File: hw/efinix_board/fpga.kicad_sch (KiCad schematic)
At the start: 1 part, among them U1 T20F256

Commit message: Start working on sdram
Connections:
- net ~{CAS}: now reaches U1.H12 (GPIOR_139)
- net ~{WE}: now reaches U1.J12 (GPIOR_141)
- net A4: now reaches U1.J13 (GPIOR_133)
- net A5: now reaches U1.J14 (GPIOR_135)
- net A6: now reaches U1.J15 (GPIOR_131)
- net A7: now reaches U1.K12 (GPIOR_148)
- net A8: now reaches U1.K14 (GPIOR_138)
- net DQ8: now reaches U1.K15 (GPIOR_136)
- net UQDM: now reaches U1.K16 (GPIOR_132)
- net A9: now reaches U1.L15 (GPIOR_147)
- net A11: now reaches U1.L16 (GPIOR_143)
- net A12: now reaches U1.M15 (GPIOR_144)
- net ~{CKE}: now reaches U1.M16 (GPIOR_145)
- net CLK: now reaches U1.P16 (GPIOR_146)
- net DQ6: now reaches U1.A11 (GPIOR_84)
- net DQ3: now reaches U1.A13 (GPIOR_95)
- net DQ1: now reaches U1.A14 (GPIOR_90)
- net DQ15: now reaches U1.A15 (GPIOR_94)
- net DQ7: now reaches U1.B10 (GPIOR_82)
- net DQ5: now reaches U1.B11 (GPIOR_83)
- net DQ4: now reaches U1.B12 (GPIOR_93)
- net DQ2: now reaches U1.B13 (GPIOR_97)
- net DQ0: now reaches U1.B14 (GPIOR_92)
- net DQ14: now reaches U1.B15 (GPIOR_98)
- net DQ13: now reaches U1.B16 (GPIOR_106)
- net LQDM: now reaches U1.B9 (GPIOR_80)
- net A2: now reaches U1.C11 (GPIOR_86)
- net A0: now reaches U1.C12 (GPIOR_85)
- net BA1: now reaches U1.C13 (GPIOR_99)
- net BA0: now reaches U1.C14 (GPIOR_102)
- net DQ12: now reaches U1.C15 (GPIOR_112)
- net Q11: now reaches U1.C16 (GPIOR_108)
- net A1: now reaches U1.D11 (GPIOR_87)
- net A10: now reaches U1.D12 (GPIOR_89)
- net ~{CS}: now reaches U1.D13 (GPIOR_103)
- net DQ10: now reaches U1.D16 (GPIOR_116)
- net A3: now reaches U1.E11 (GPIOR_88)
- net ~{RAS}: now reaches U1.E12 (GPIOR_91)
- net DQ9: now reaches U1.E16 (GPIOR_119)
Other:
- moved on the sheet: U1B, U1C, U1D, U1F, U1H

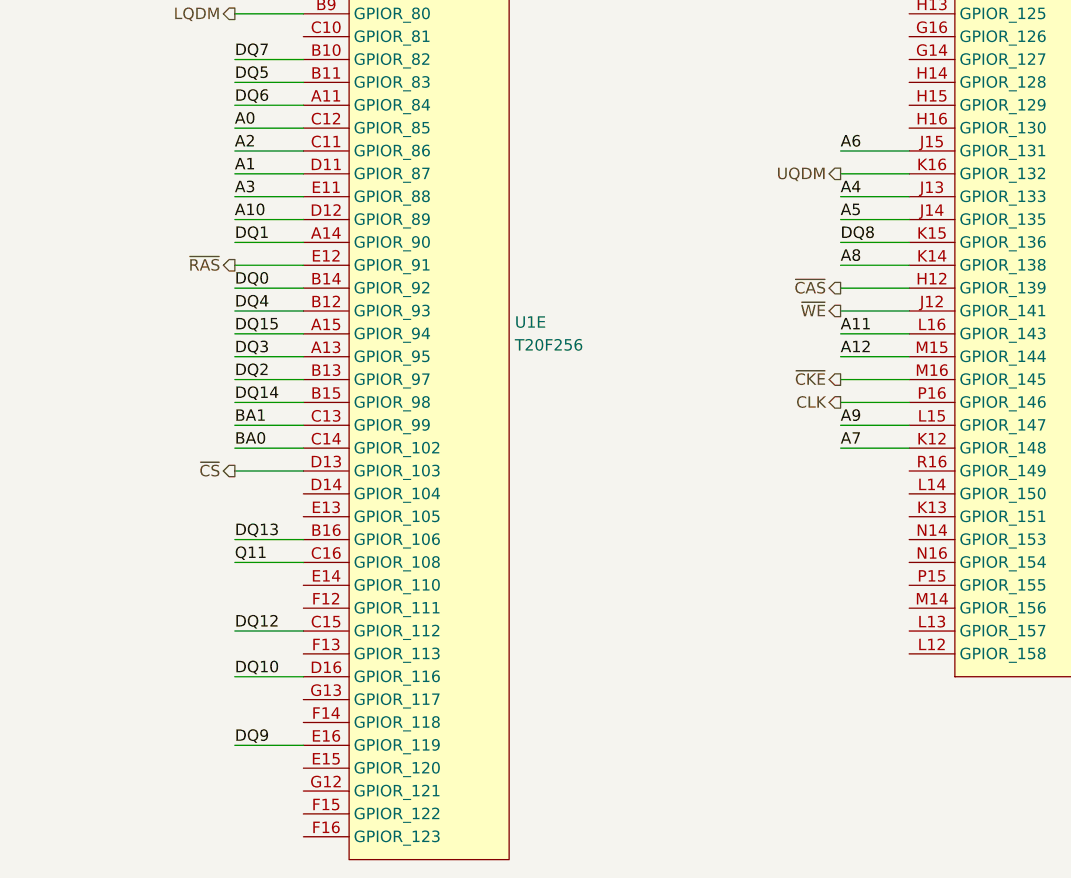
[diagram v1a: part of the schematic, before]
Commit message: More sdram routing
This changes the pinout from the development board, now DQ8 and UDQM are
different.
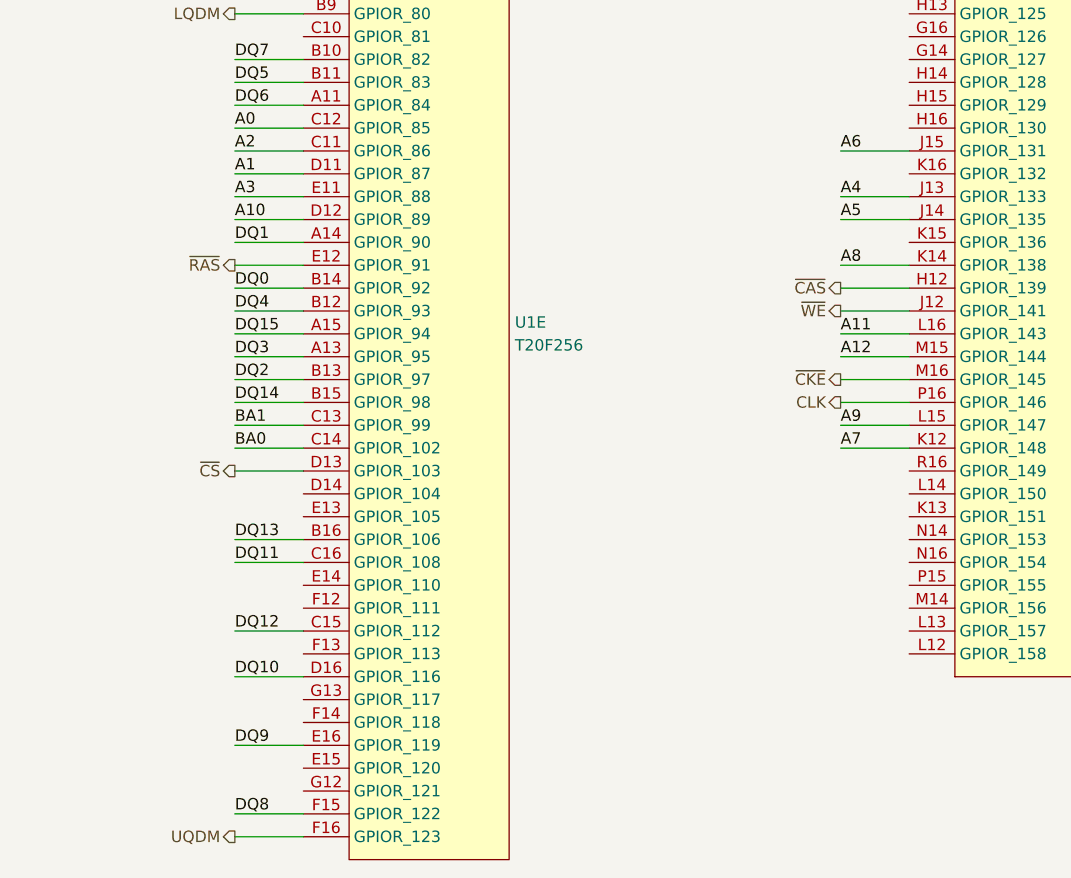
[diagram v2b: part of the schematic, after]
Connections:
- net Q11 is gone; now on net DQ11: U1.C16 (GPIOR_108)
- net DQ8: now also U1.F15 (GPIOR_122); no longer U1.K15 (GPIOR_136)
- net UQDM: now also U1.F16 (GPIOR_123); no longer U1.K16 (GPIOR_132)
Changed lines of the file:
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@@
     (stroke (width 0) (type default) (color 0 0 0 0))
   )
-  (wire (pts (xy 168.91 97.79) (xy 161.29 97.79))
+  (wire (pts (xy 101.6 161.29) (xy 93.98 161.29))
     (stroke (width 0) (type default) (color 0 0 0 0))
   )
@@
     (stroke (width 0) (type default) (color 0 0 0 0))
   )
-  (wire (pts (xy 168.91 90.17) (xy 161.29 90.17))
+  (wire (pts (xy 101.6 163.83) (xy 93.98 163.83))
     (stroke (width 0) (type default) (color 0 0 0 0))
   )
@@
     (effects (font (size 1.27 1.27)) (justify right bottom))
   )
-  (label "DQ8" (at 161.29 97.79 0)
+  (label "DQ8" (at 93.98 161.29 0)
     (effects (font (size 1.27 1.27)) (justify left bottom))
   )
@@
     (effects (font (size 1.27 1.27)) (justify left bottom))
   )
-  (label "Q11" (at 93.98 133.35 0)
+  (label "DQ11" (at 93.98 133.35 0)
     (effects (font (size 1.27 1.27)) (justify left bottom))
   )
@@
     (effects (font (size 1.27 1.27)) (justify right))
   )
-  (hierarchical_label "UQDM" (shape output) (at 161.29 90.17 180)
-    (effects (font (size 1.27 1.27)) (justify right))
-  )
+  (hierarchical_label "UQDM" (shape output) (at 93.98 163.83 180)
+    (effects (font (size 1.27 1.27)) (justify right))
+  )

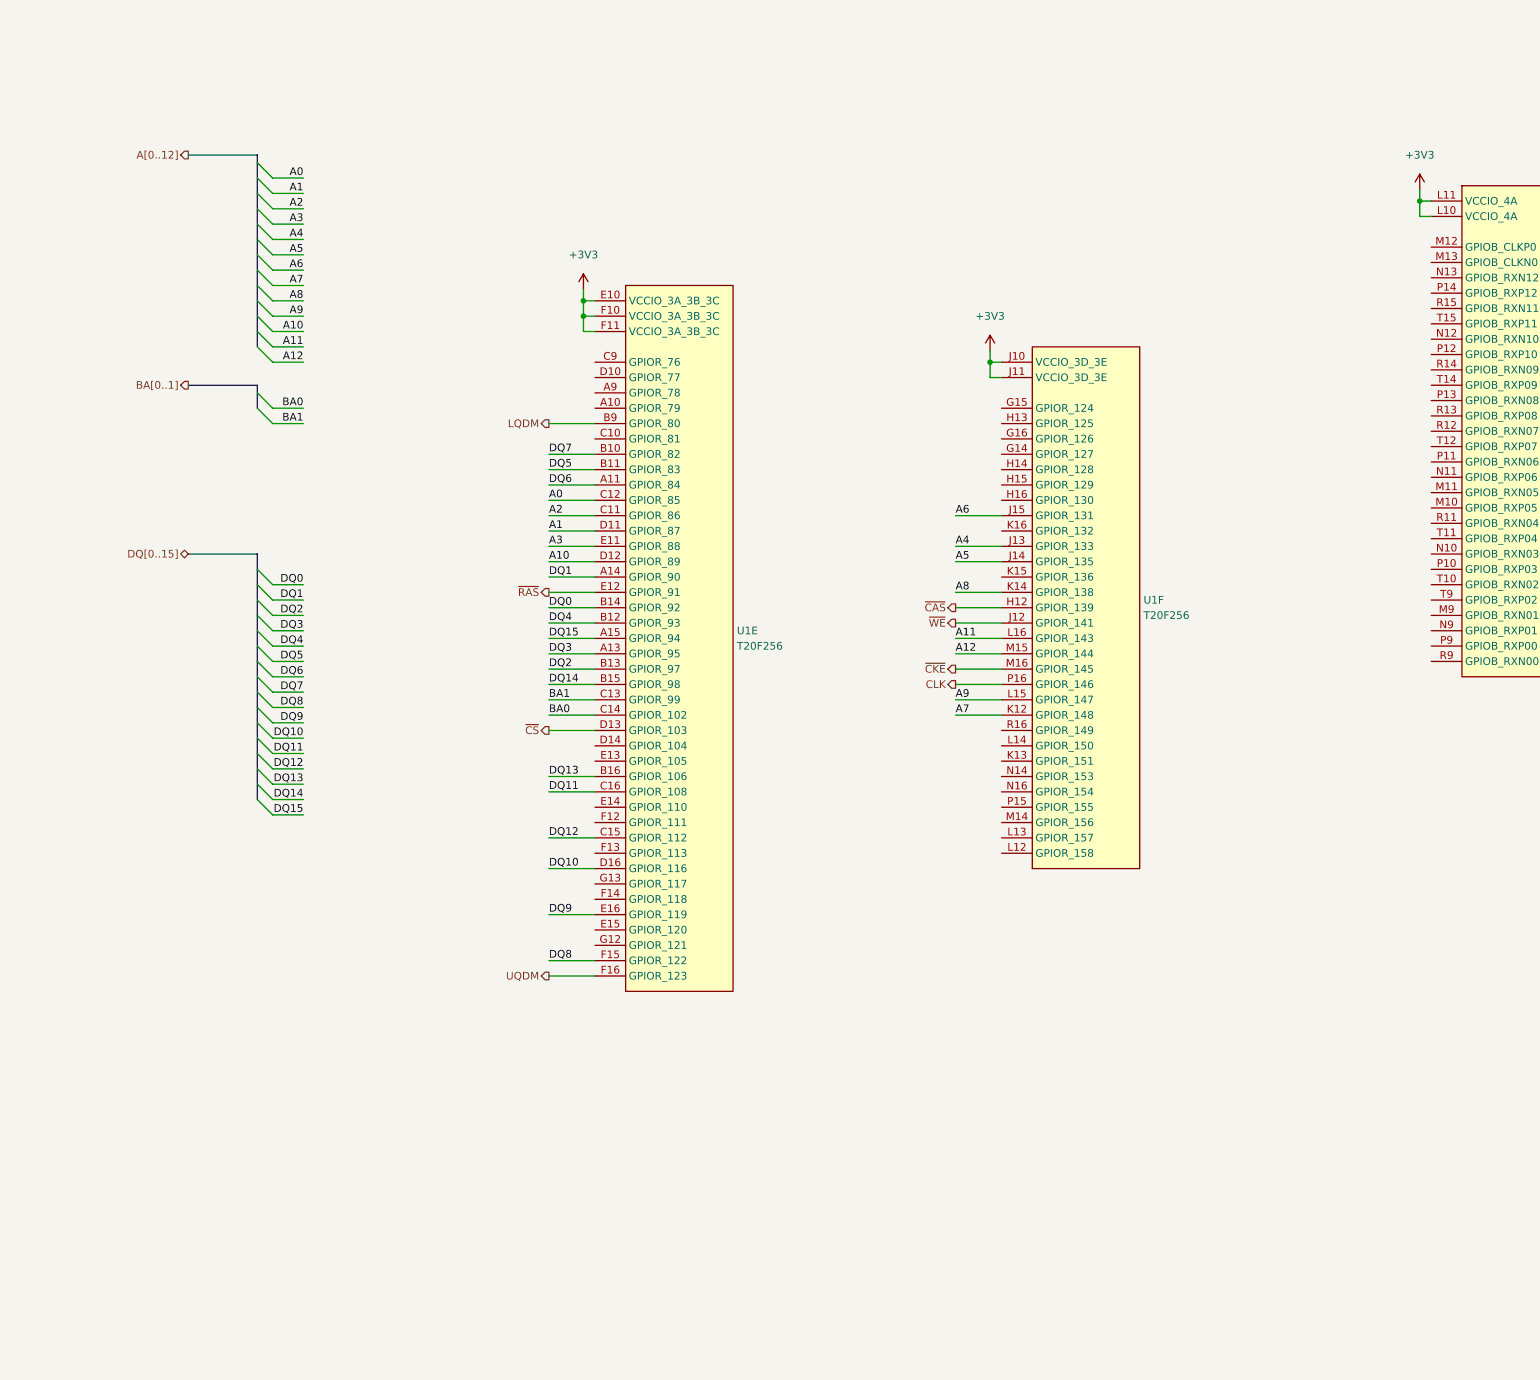
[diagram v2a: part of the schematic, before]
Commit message: Add CPU and begin sch/layout
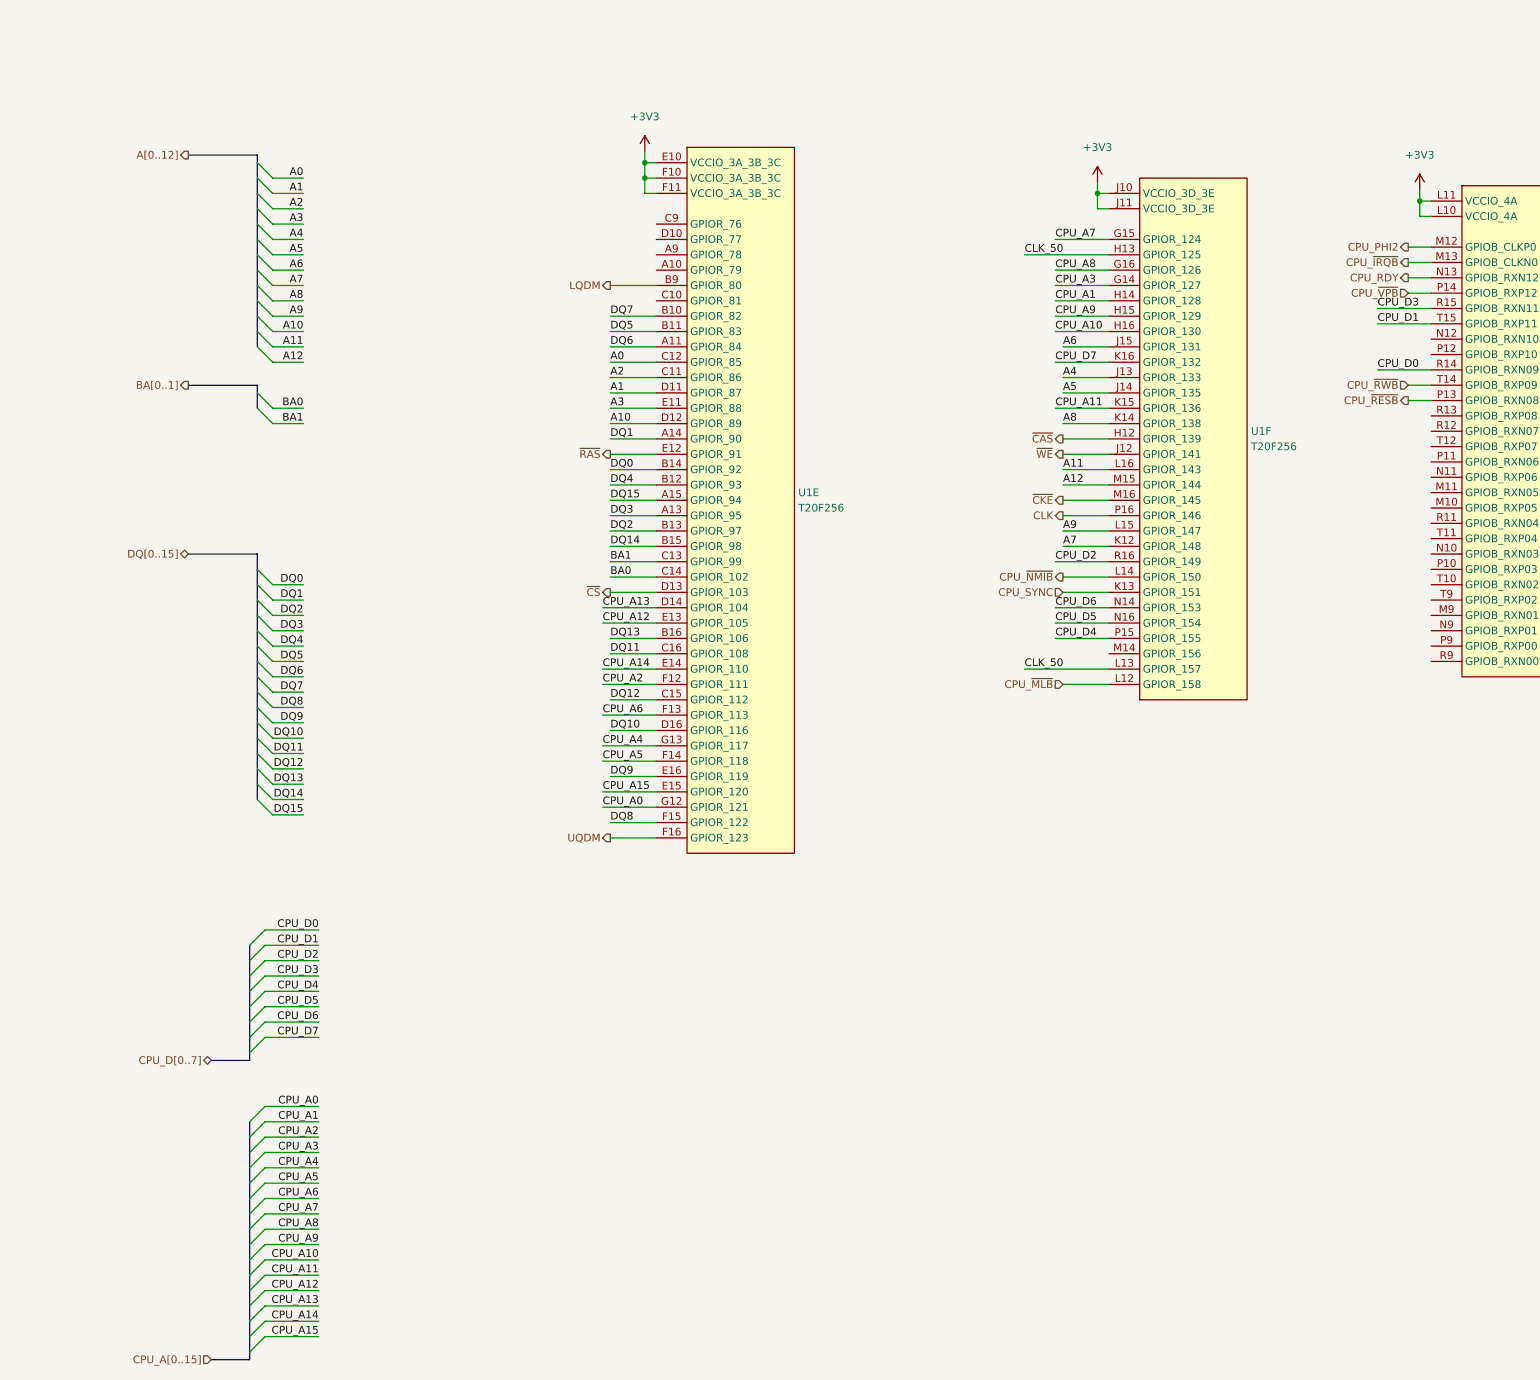
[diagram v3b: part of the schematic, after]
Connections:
- net CPU_A3: now reaches U1.G14 (GPIOR_127)
- net CPU_A7: now reaches U1.G15 (GPIOR_124)
- net CPU_A8: now reaches U1.G16 (GPIOR_126)
- net CLK_50: now reaches U1.H13 (GPIOR_125)
- net CLK_50: now also U1.L13 (GPIOR_157)
- net CPU_A1: now reaches U1.H14 (GPIOR_128)
- net CPU_A9: now reaches U1.H15 (GPIOR_129)
- net CPU_A10: now reaches U1.H16 (GPIOR_130)
- net CPU_SYNC: now reaches U1.K13 (GPIOR_151)
- net CPU_A11: now reaches U1.K15 (GPIOR_136)
- net CPU_D7: now reaches U1.K16 (GPIOR_132)
- net CPU_~{MLB}: now reaches U1.L12 (GPIOR_158)
- net CPU_~{NMIB}: now reaches U1.L14 (GPIOR_150)
- net CPU_D6: now reaches U1.N14 (GPIOR_153)
- net CPU_D5: now reaches U1.N16 (GPIOR_154)
- net CPU_D4: now reaches U1.P15 (GPIOR_155)
- net CPU_D2: now reaches U1.R16 (GPIOR_149)
- net CPU_A13: now reaches U1.D14 (GPIOR_104)
- net CPU_A12: now reaches U1.E13 (GPIOR_105)
- net CPU_A14: now reaches U1.E14 (GPIOR_110)
- net CPU_A15: now reaches U1.E15 (GPIOR_120)
- net CPU_A2: now reaches U1.F12 (GPIOR_111)
- net CPU_A6: now reaches U1.F13 (GPIOR_113)
- net CPU_A5: now reaches U1.F14 (GPIOR_118)
- net CPU_A0: now reaches U1.G12 (GPIOR_121)
- net CPU_A4: now reaches U1.G13 (GPIOR_117)
- net CPU_PHI2: now reaches U1.M12 (GPIOB_CLKP0)
- net CPU_~{IRQB}: now reaches U1.M13 (GPIOB_CLKN0)
- net CPU_RDY: now reaches U1.N13 (GPIOB_RXN12)
- net CPU_~{RESB}: now reaches U1.P13 (GPIOB_RXN08)
- net CPU_~{VPB}: now reaches U1.P14 (GPIOB_RXP12)
- net CPU_D0: now reaches U1.R14 (GPIOB_RXN09)
- net CPU_D3: now reaches U1.R15 (GPIOB_RXN11)
- net CPU_~{RWB}: now reaches U1.T14 (GPIOB_RXP09)
- net CPU_D1: now reaches U1.T15 (GPIOB_RXP11)
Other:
- moved on the sheet: U1E, U1F

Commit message: Update schematics and board
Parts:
- removed unit 2 of U1
